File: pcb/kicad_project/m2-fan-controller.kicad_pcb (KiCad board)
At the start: 2 copper layers, 22 x 30 mm, 18 parts, among them J1 Bus_M.2_Socket_E, J2 Conn_01x04, J3 Conn_01x04, J4 JST PH_S2B-PH-K, J5 Conn_02x02_Odd_Even, U1 STM32F042F6P6

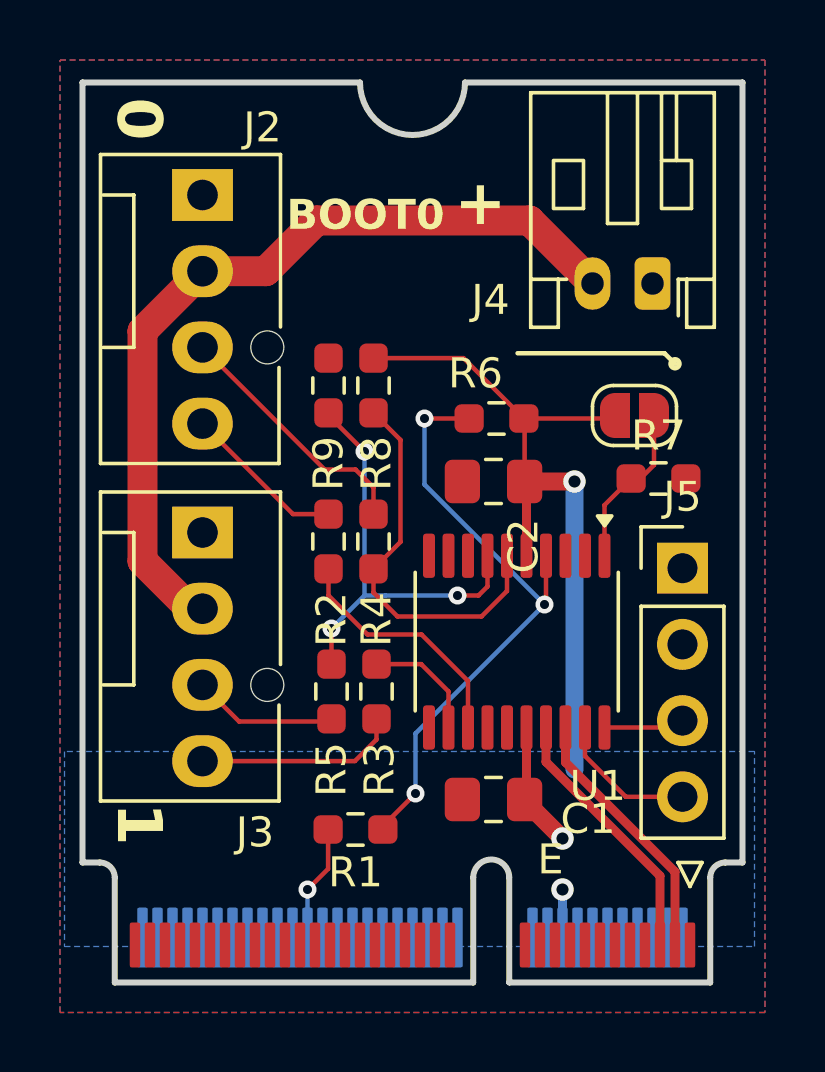
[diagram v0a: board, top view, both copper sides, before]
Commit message: Implement power control for fans (#1)
* Final revision

* Use 0603 components
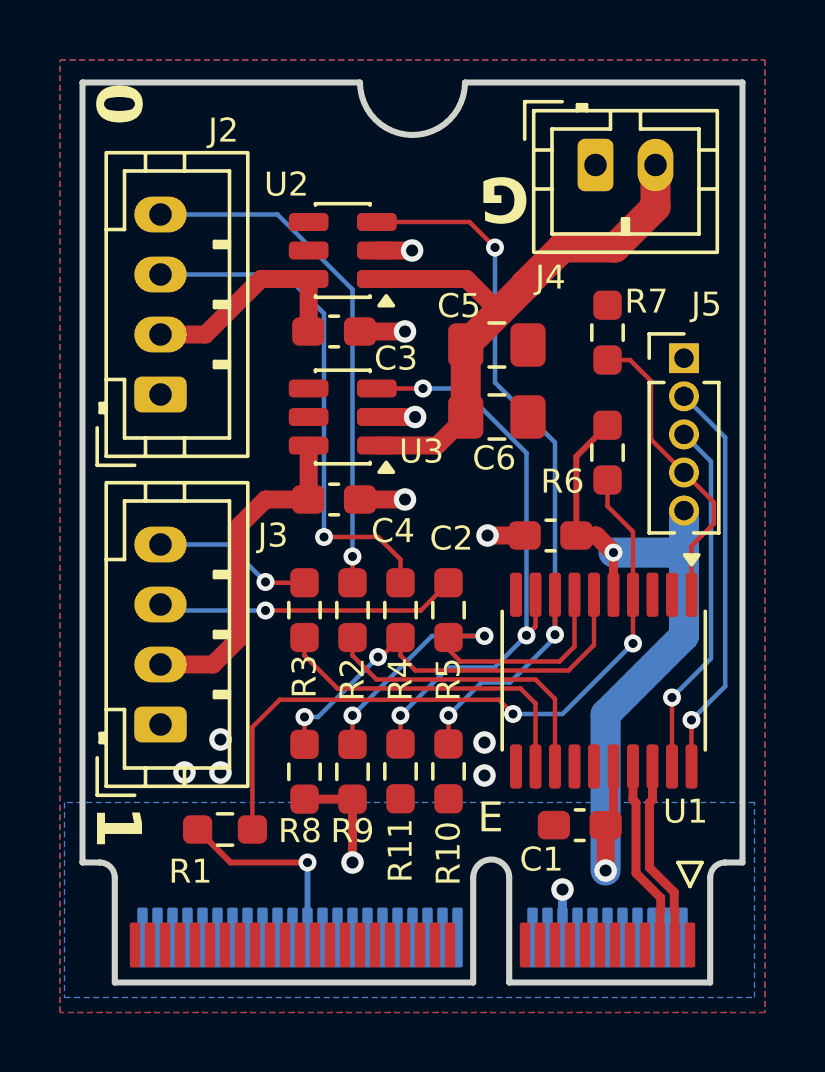
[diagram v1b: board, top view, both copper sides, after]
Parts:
- removed JP1: Jumper_2_Open, Jumper:SolderJumper-2_P1.3mm_Open_RoundedPad1.0x1.5mm
- added C3: 0.1uF, Capacitor_SMD:C_0603_1608Metric_Pad1.08x0.95mm_HandSolder, F.Cu at (136.4, 88.3)
- added C4: 0.1uF, Capacitor_SMD:C_0603_1608Metric_Pad1.08x0.95mm_HandSolder, F.Cu at (136.4, 93.9)
- added C5: 1uF, Capacitor_SMD:C_0805_2012Metric_Pad1.18x1.45mm_HandSolder, F.Cu at (141.8, 88.8)
- added C6: 1uF, Capacitor_SMD:C_0805_2012Metric_Pad1.18x1.45mm_HandSolder, F.Cu at (141.8, 91.2)
- added R10: 10kOhm, Resistor_SMD:R_0603_1608Metric_Pad0.98x0.95mm_HandSolder, F.Cu at (140.2, 103.0)
- added R11: 10kOhm, Resistor_SMD:R_0603_1608Metric_Pad0.98x0.95mm_HandSolder, F.Cu at (138.6, 103.0)
- added U2: TPS22810DBV, Package_TO_SOT_SMD:SOT-23-6, F.Cu at (136.7, 85.6)
- added U3: TPS22810DBV, Package_TO_SOT_SMD:SOT-23-6, F.Cu at (136.7, 91.2)
- C1, C2: footprint Capacitor_SMD:C_0805_2012Metric_Pad1.18x1.45mm_HandSolder -> Capacitor_SMD:C_0603_1608Metric_Pad1.08x0.95mm_HandSolder
- J2, J3: value Conn_01x04 -> JST PH_B4B-PH-K; footprint Connector:FanPinHeader_1x04_P2.54mm_Vertical -> Connector_JST:JST_PH_B4B-PH-K_1x04_P2.00mm_Vertical
- J4: footprint Connector_JST:JST_PH_S2B-PH-K_1x02_P2.00mm_Horizontal -> Connector_JST:JST_PH_B2B-PH-K_1x02_P2.00mm_Vertical
- J5: footprint Connector_PinHeader_2.54mm:PinHeader_1x04_P2.54mm_Vertical -> Connector_PinHeader_1.27mm:PinHeader_1x05_P1.27mm_Vertical
- moved R8 13.1 mm to (135.4, 103.0), turned to 90 degrees
- moved R9 12.9 mm to (137.0, 103.0), turned to 90 degrees
- moved J5 7.00 mm to (148.1, 89.2)
- moved J2 6.80 mm to (130.6, 90.4), turned to 90 degrees
- moved J3 6.55 mm to (130.6, 101.4), turned to 90 degrees
- moved R7 5.15 mm to (145.5, 88.3), turned to 90 degrees
- moved R5 4.75 mm to (140.2, 97.6), turned to 90 degrees
- moved J4 4.38 mm to (145.1, 82.8), turned to 0 degrees
- moved R1 4.35 mm to (132.8, 104.9)
- moved R6 3.87 mm to (145.5, 92.3), turned to -90 degrees
- moved R3 3.62 mm to (135.4, 97.6), turned to 90 degrees
- moved U1 3.18 mm to (145.4, 99.9)
- moved C1 3.00 mm to (144.6, 104.8)
- moved C2 2.62 mm to (143.6, 95.1)
- moved R4 2.46 mm to (138.6, 97.6)
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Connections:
- J2 pad 2: +12V -> Net-(J2-Pin_2)
- J3 pad 2: +12V -> Net-(J3-Pin_2)
- J5 pad 2: +3.3V -> SWCLK
- J5 pad 3: SWCLK -> SWDIO
- J5 pad 4: SWDIO -> BOOT0
- U1 pad 8: unconnected-(U1-PA2-Pad8) -> EN_0
- U1 pad 9: unconnected-(U1-PA3-Pad9) -> EN_1
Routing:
- net EN_0: track 0.00 -> 24.8 mm, vias 0 -> 3
- net EN_1: track 0.00 -> 19.4 mm, vias 0 -> 3
- net Net-(J2-Pin_4): track 5.45 -> 17.2 mm, vias 0 -> 1
- net Net-(J3-Pin_2): track 0.00 -> 11.2 mm
- net SWCLK: track 2.70 -> 13.4 mm, vias 0 -> 1
- net Net-(J2-Pin_3): track 8.55 -> 17.1 mm, vias 0 -> 1
- net +12V: track 27.6 -> 19.9 mm
- net Net-(J2-Pin_2): track 0.00 -> 7.45 mm
- net SWDIO: track 4.76 -> 12.0 mm, vias 0 -> 1
- net PWM_1: track 3.98 -> 11.1 mm
- net GND: track 1.60 -> 7.94 mm, vias 1 -> 11
- net Net-(J3-Pin_3): track 4.31 -> 10.1 mm, vias 0 -> 1
- net BOOT0: track 5.94 -> 10.0 mm
- net Net-(J1-~{PERST0}): track 3.88 -> 6.62 mm
- net USB_D-: track 8.82 -> 6.34 mm
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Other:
- board text added: "12V"
- board text added: "3.3V"
- board text added: "G"
- board text added: "GND"
- board text added: "PCB thickness 0.8 mm"
- board text added: "PWM"
- board text added: "SWCLK"
- board text added: "SWDIO"
- board text added: "TACH"
- board text removed: "+"
- board text removed: "M.2 fan controller"
